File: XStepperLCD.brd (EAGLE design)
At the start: 49.5 x 48.3 mm, 28 parts, among them Q2 16 MHZ, U1 LCD-16X2NOHOLES

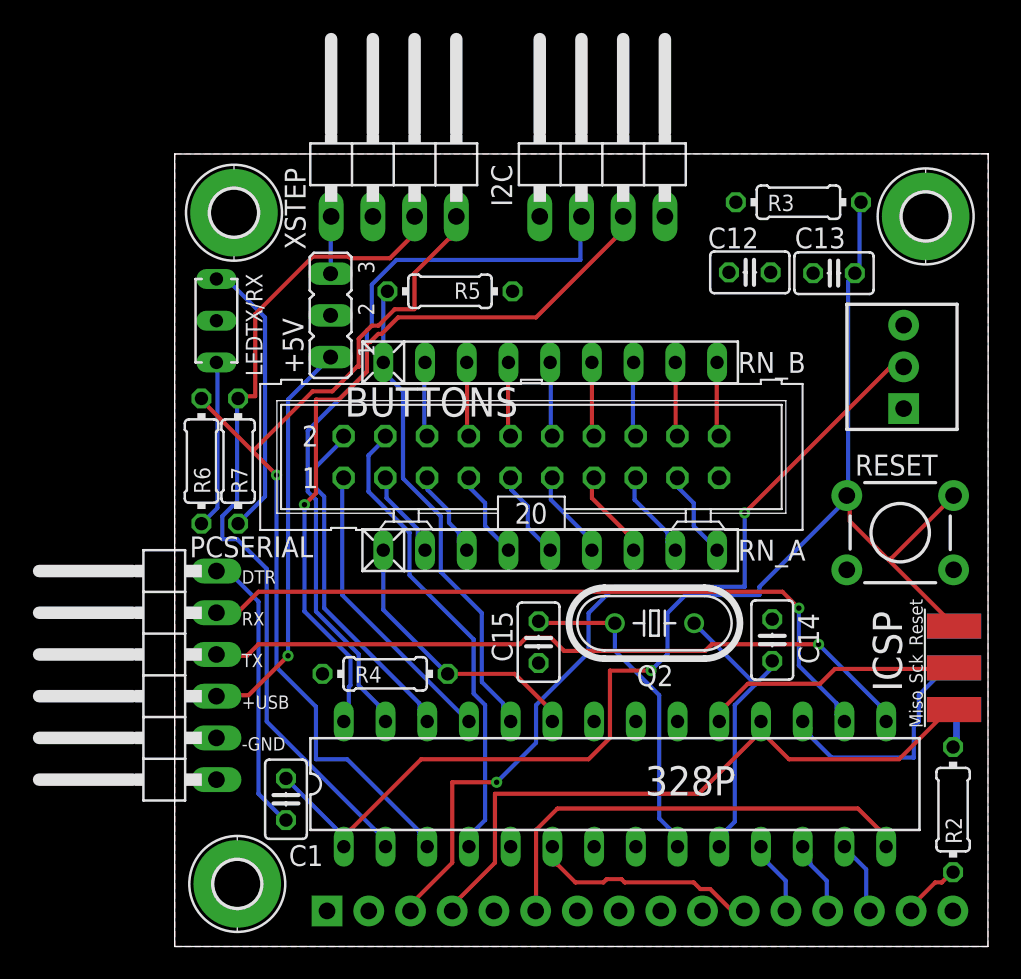
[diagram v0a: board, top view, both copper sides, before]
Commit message: - damn, misstake with branches work on master
- add a lot changes for LCDMenu
- use phi_interfaces for analog buttons
- remove a lot unused code
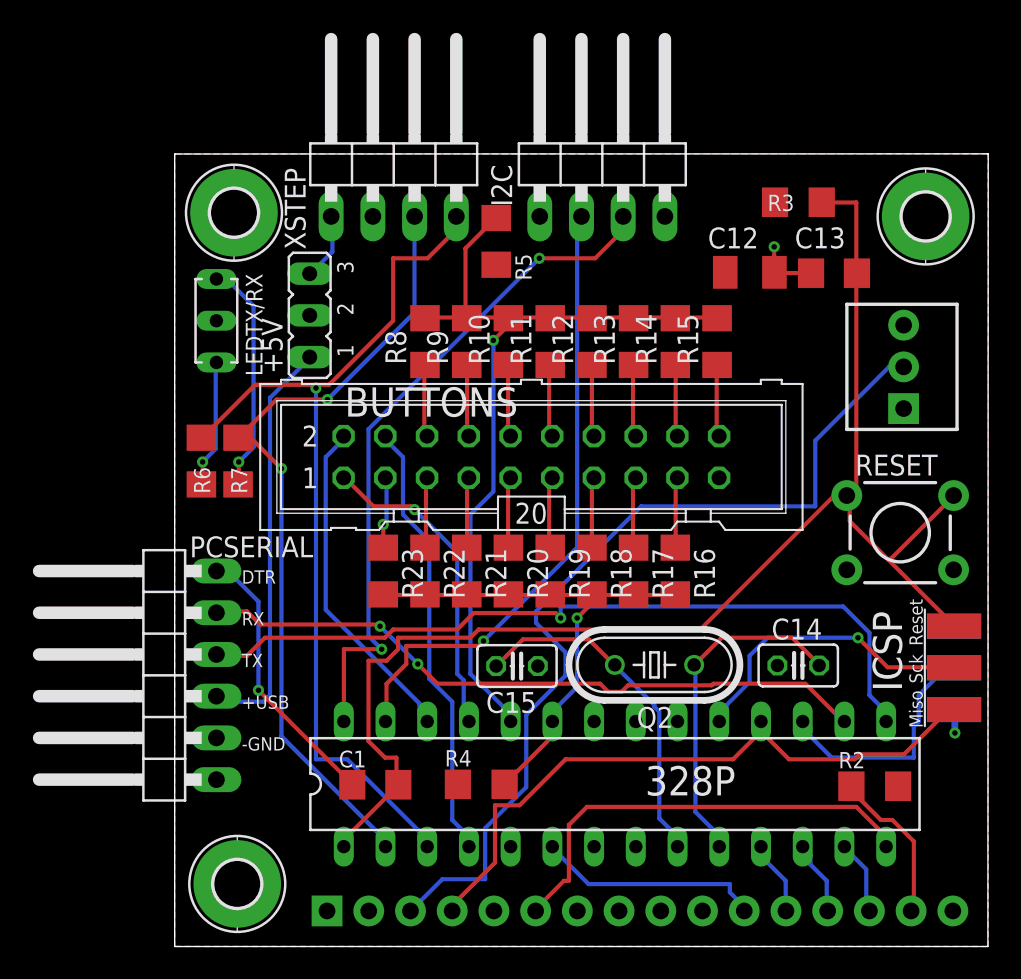
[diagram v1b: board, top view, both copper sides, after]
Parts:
- removed RN_A, RN_B: 680, resistor-net:RN-9
- added R10, R11, R12, R13, R14, R15, R16, R17, R18, R19, R20, R21, R22, R23, R8, R9: 680, resistor:R1206
- C1, C13: device resistor:C025-025X050 -> resistor:C1206
- C12: device resistor:C025-025X050 -> resistor:C1206K
- R2, R3, R4, R5, R6, R7: device resistor:0204/7 -> resistor:R1206
- moved R4 8.91 mm to (18.7, 9.88)
- moved C1 5.51 mm to (12.2, 9.85), turned to 0 degrees
- moved R2 4.97 mm to (42.6, 9.76), turned to 180 degrees
- moved R5 4.14 mm to (19.6, 42.9), turned to 270 degrees
- moved Q2 2.54 mm to (29.2, 17.1)
- moved C14 2.22 mm to (38.0, 17.1), turned to 180 degrees
- moved C15 1.96 mm to (20.8, 17.1), turned to 0 degrees
- moved +5V 1.27 mm to (8.22, 38.4)
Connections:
- net BUTTONS_A: now also R16.2, R17.2, R18.2, R19.2, R20.2, R21.2, R22.2, R23.2; no longer RN_A.1
- net BUTTONS_B: now also R10.2, R11.2, R12.2, R13.2, R14.2, R15.2, R8.2, R9.2; no longer RN_B.1
- net N$10: now also R22.1; no longer RN_A.3
- net N$11: now also R10.1; no longer RN_B.4
- net N$12: now also R11.1; no longer RN_B.5
- net N$13: now also R12.1; no longer RN_B.6
- net N$15: now also R13.1; no longer RN_B.7
- net N$16: now also R21.1; no longer RN_A.4
- net N$17: now also R20.1; no longer RN_A.5
- net N$18: now also R19.1; no longer RN_A.6
- net N$19: now also R14.1; no longer RN_B.8
- net N$20: now also R15.1; no longer RN_B.9
- net N$4: now also R18.1; no longer RN_A.7
- net N$5: now also R17.1; no longer RN_A.8
- net N$6: now also R16.1; no longer RN_A.9
- net N$7: now also R8.1; no longer RN_B.2
- net N$8: now also R9.1; no longer RN_B.3
- net N$9: now also R23.1; no longer RN_A.2
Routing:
- net BUTTONS_B: track 29.5 -> 52.0 mm, vias 0 -> 1
- net BUTTONS_A: track 17.3 -> 32.3 mm, vias 0 -> 1
- net SDA: track 46.2 -> 38.3 mm, vias 0 -> 1
- net N$2: track 3.70 -> 9.96 mm
- net SCL: track 46.1 -> 41.8 mm, vias 1 -> 2
- net USB_TXD: track 44.1 -> 48.2 mm
- net GND: track 0.00 -> 3.79 mm, vias 0 -> 1
- net USB_RXD: track 44.5 -> 41.5 mm, vias 1 -> 2
- net N$22: track 17.2 -> 14.2 mm, vias 0 -> 1
- net N$1: track 52.4 -> 55.3 mm, vias 2 -> 0
- net N$34: track 17.9 -> 20.7 mm
- net N$21: track 10.2 -> 7.80 mm, vias 0 -> 1
- net TX: track 51.5 -> 49.1 mm, vias 0 -> 2
- net SCK: track 16.2 -> 18.5 mm, vias 0 -> 1
- net POT_A: track 28.8 -> 27.1 mm
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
